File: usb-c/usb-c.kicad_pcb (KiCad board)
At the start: 2 copper layers, 86.4 x 15.2 mm, 34 parts, among them J1 USB_C, J2 SWD, J3 OUTPUT, Q1 MMBT3904, Q2 DMP3017SFG, SW1 SWITCH, U1 FUSB302B11MPX, U2 AP2204R-3.3, U3 STM32F072C8Ux

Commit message: update
Signed-off-by: Jess Frazelle <jess@oxide.computer>
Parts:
- moved C1 46.0 mm to (143.5, 54.6), turned to 90 degrees
- moved U2 42.7 mm to (139.7, 47.0), turned to 90 degrees
- moved U3 40.0 mm to (104.8, 50.1)
- moved R1 36.4 mm to (148.6, 53.3), turned to 270 degrees
- moved R8 29.4 mm to (151.1, 50.8), turned to 180 degrees
- moved R3 29.0 mm to (106.7, 55.9), turned to 90 degrees
- moved R2 28.4 mm to (104.1, 55.9), turned to 90 degrees
- moved R6 27.9 mm to (158.8, 47.0), turned to 270 degrees
- moved C9 25.5 mm to (139.7, 54.6), turned to 270 degrees
- moved C7 25.2 mm to (135.9, 54.6), turned to 270 degrees
- moved R4 25.0 mm to (144.8, 48.3), turned to 270 degrees
- moved C11 23.7 mm to (113.0, 52.1), turned to 270 degrees
- moved C5 23.6 mm to (130.8, 54.6), turned to 90 degrees
- moved U1 23.3 mm to (92.7, 52.1), turned to 90 degrees
- moved C8 22.9 mm to (127.0, 54.6), turned to 90 degrees
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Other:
- board outline removed

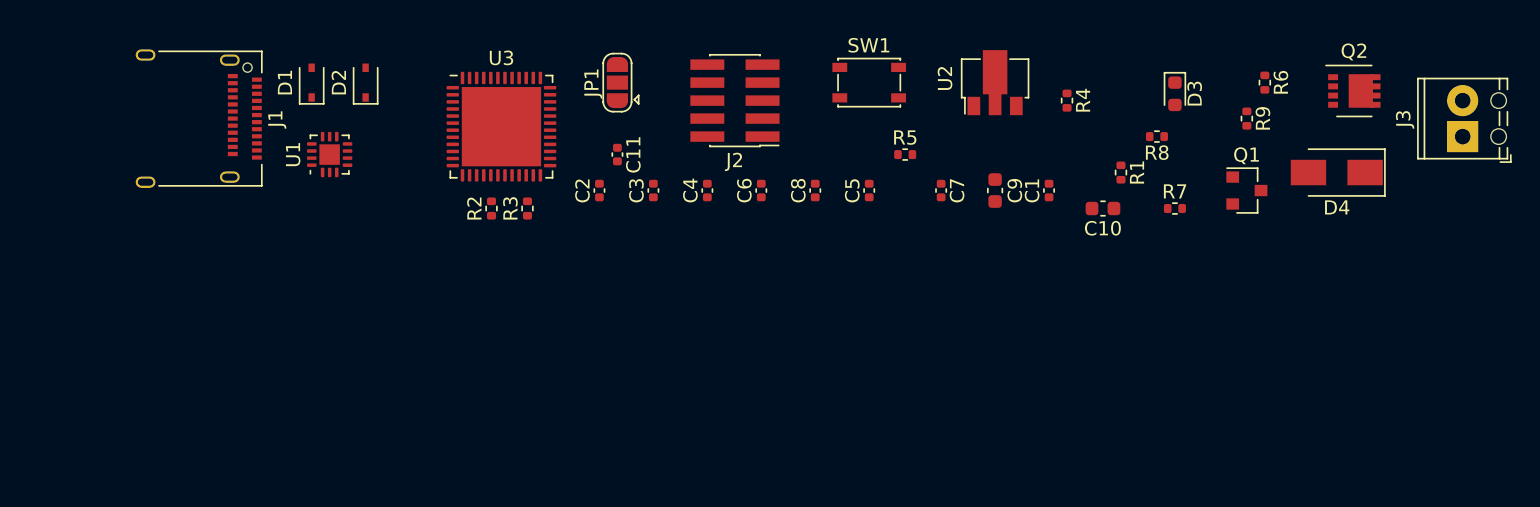
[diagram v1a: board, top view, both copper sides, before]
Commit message: update dongle
Signed-off-by: Jess Frazelle <jess@oxide.computer>
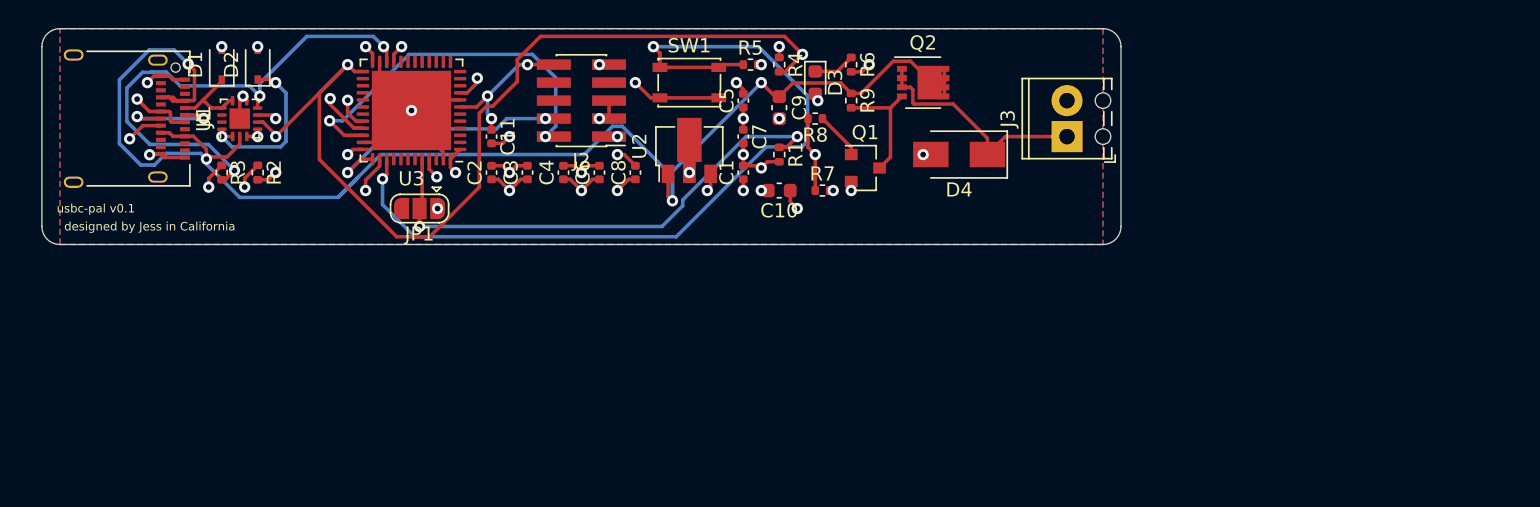
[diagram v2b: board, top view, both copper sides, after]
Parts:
- moved Q2 30.5 mm to (134.6, 47.0)
- moved R6 29.2 mm to (129.5, 45.7)
- moved R9 28.0 mm to (129.5, 48.3)
- moved J3 27.9 mm to (144.8, 50.8)
- moved Q1 27.0 mm to (130.5, 53.0)
- moved D4 26.7 mm to (137.2, 52.1)
- moved D3 25.4 mm to (127.0, 47.0)
- moved R7 24.9 mm to (127.5, 54.6)
- moved R1 24.2 mm to (124.5, 52.1)
- moved R8 24.2 mm to (127.0, 49.5)
- moved C10 22.9 mm to (124.5, 54.6)
- moved U2 22.1 mm to (118.1, 51.8)
- moved R3 21.7 mm to (85.1, 53.3), turned to 270 degrees
- moved C1 21.6 mm to (121.9, 53.3)
- moved R4 20.5 mm to (124.5, 45.7)
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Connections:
- SW1 pad 2: /SETUP -> +3V3
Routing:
- net GND: track 0.00 -> 175.4 mm, vias 0 -> 23
- net +3V3: track 0.00 -> 118.6 mm, vias 0 -> 18
- net VBUS: track 0.00 -> 109.4 mm, vias 0 -> 4
- net INT_N: track 0.00 -> 66.6 mm, vias 0 -> 3
- net /SETUP: track 0.00 -> 60.2 mm, vias 0 -> 2
- net OUT_CTRL: track 0.00 -> 58.8 mm, vias 0 -> 2
- net Net-(D3-Pad2): track 0.00 -> 49.8 mm, vias 0 -> 2
- net SDA: track 0.00 -> 36.6 mm, vias 0 -> 3
- net /BOOT: track 0.00 -> 36.0 mm, vias 0 -> 2
- net /SWDIO: track 0.00 -> 26.4 mm, vias 0 -> 2
- net D+: track 0.00 -> 26.0 mm, vias 0 -> 3
- net SCL: track 0.00 -> 24.0 mm, vias 0 -> 3
- net D-: track 0.00 -> 23.8 mm, vias 0 -> 2
- net Net-(D2-Pad1): track 0.00 -> 21.3 mm, vias 0 -> 3
- net /SWCLK: track 0.00 -> 18.3 mm, vias 0 -> 2
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- added copper zone on B.Cu, net (none)
- added copper zone on F.Cu, net (none)
- added copper zone on PWR, net +3V3
- added copper zone on GND, net GND
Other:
- board outline added: 76.2 x 15.2 mm
- copper layers 2 -> 4
- board text added: "designed by Jess in California"
- board text added: "usbc-pal v0.1"

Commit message: fix typo
Signed-off-by: Jess Frazelle <jess@oxide.computer>
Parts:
- D2: value MM325V6T1G -> MM3Z5V6T1G

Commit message: updates
Signed-off-by: Jess Frazelle <jess@oxide.computer>
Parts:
- JP1: footprint Jumper:SolderJumper-3_P1.3mm_Open_RoundedPad1.0x1.5mm -> Jumper:SolderJumper-2_P1.3mm_Open_RoundedPad1.0x1.5mm
